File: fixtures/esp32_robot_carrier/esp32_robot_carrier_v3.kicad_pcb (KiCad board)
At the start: 2 copper layers, 128 x 189 mm, 157 parts, among them J3V3 3V3_AUX, J3V3_1 3V3_RAIL_1, J3V3_2 3V3_RAIL_2, J3V3_3 3V3_RAIL_3, J3V3_4 3V3_RAIL_4, Q5 STP100N10F7_100V, Q6 STP100N10F7_100V, U10 TLV9002IDR_DUAL_THROTTLE_RRIO, U4 LTC4367IMS8#PBF, U6 AQY212SX_60V_0.5A_PHOTOMOS, U7 AQY212SX_60V_0.5A_PHOTOMOS, U8 AQY212SX_60V_0.5A_PHOTOMOS, U9 AQY212SX_60V_0.5A_PHOTOMOS

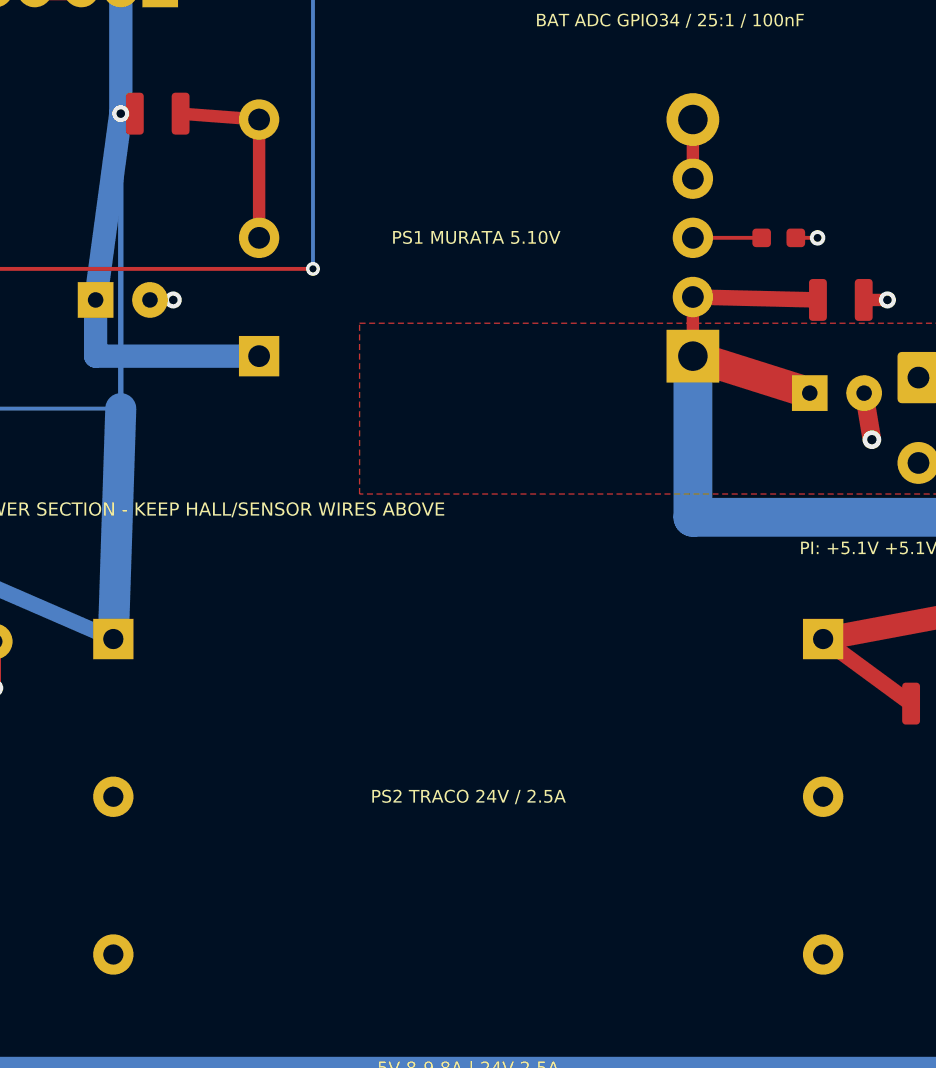
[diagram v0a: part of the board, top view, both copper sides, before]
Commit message: Replace carrier DC-DC bricks with external buck terminals
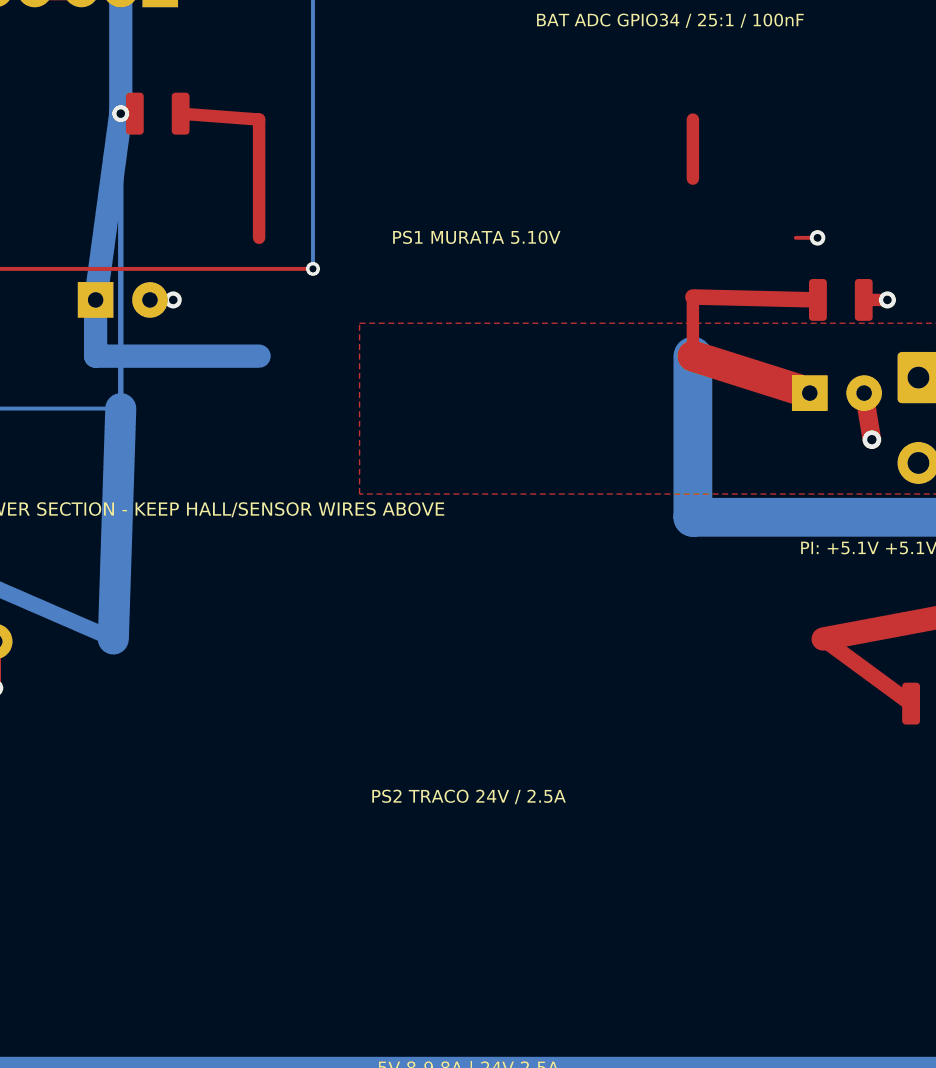
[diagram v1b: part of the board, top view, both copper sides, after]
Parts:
- removed PS1: UWS-5/10-Q48N-C_18-75VIN_5V_10A, Murata_UWS_Q48_THT
- removed PS2: TEN_60-4815WIN_18-75VIN_24V_2.5A, Traco_TEN60WIN_THT
- removed R44: 806k_1pct_UWS_TRIM_5V1, R_0805_2012Metric
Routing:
- net UWS_TRIM: track 4.43 -> 0.00 mm
